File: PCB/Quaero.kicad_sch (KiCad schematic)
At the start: 61 parts, among them J1 USB_C_Receptacle_USB2.0_16P, J2 OLED_128x32, J5 Conn_01x02, SW2 SW_SPDT

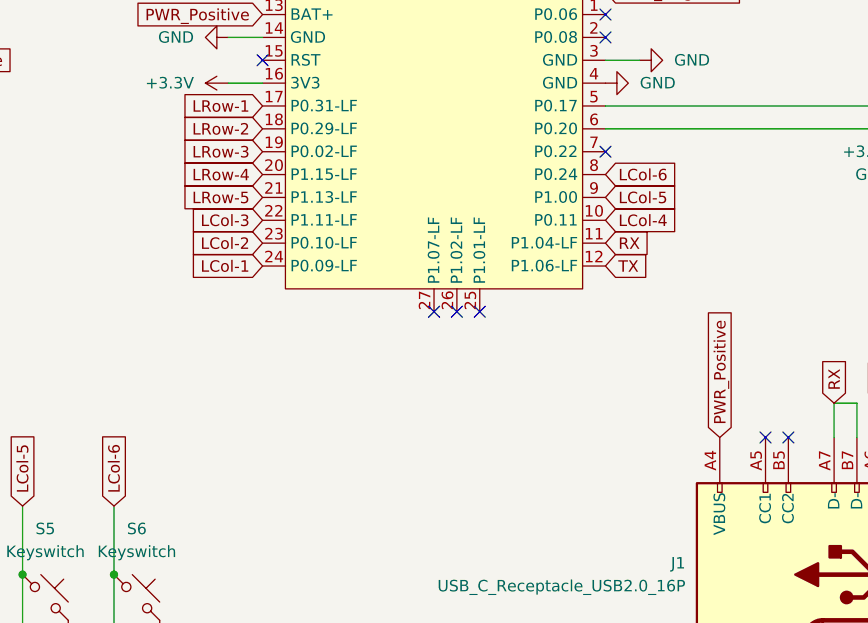
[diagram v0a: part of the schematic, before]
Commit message: Left side partial routing attempt 4
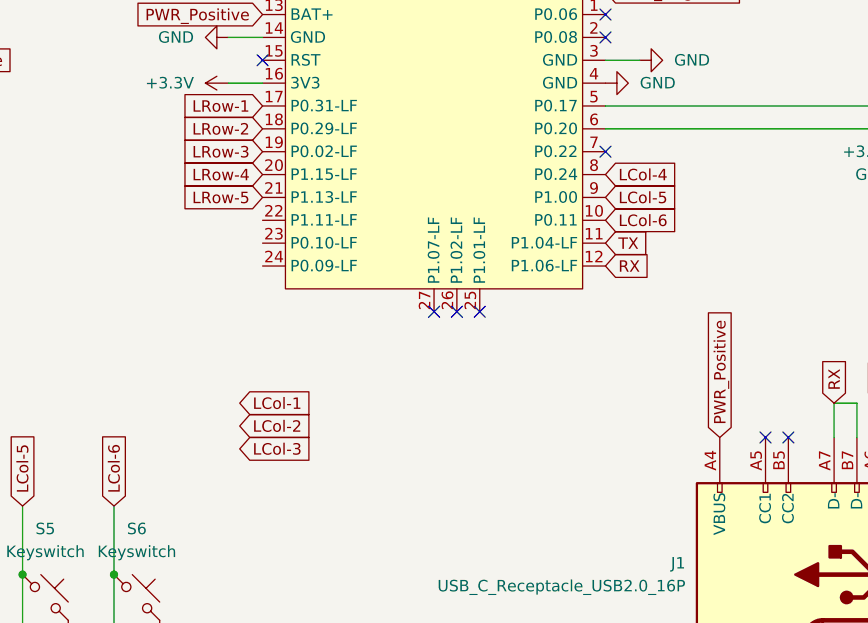
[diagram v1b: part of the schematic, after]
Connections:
- net LCol-1: no longer MCUL1.24 (P0.09-LF)
- net LCol-2: no longer MCUL1.23 (P0.10-LF)
- net LCol-3: no longer MCUL1.22 (P1.11-LF)
- net LCol-4: now also MCUL1.8 (P0.24); no longer MCUL1.10 (P0.11)
- net LCol-6: now also MCUL1.10 (P0.11); no longer MCUL1.8 (P0.24)
- net RX: now also MCUL1.12 (P1.06-LF); no longer MCUL1.11 (P1.04-LF)
- net TX: now also MCUL1.11 (P1.04-LF); no longer MCUL1.12 (P1.06-LF)

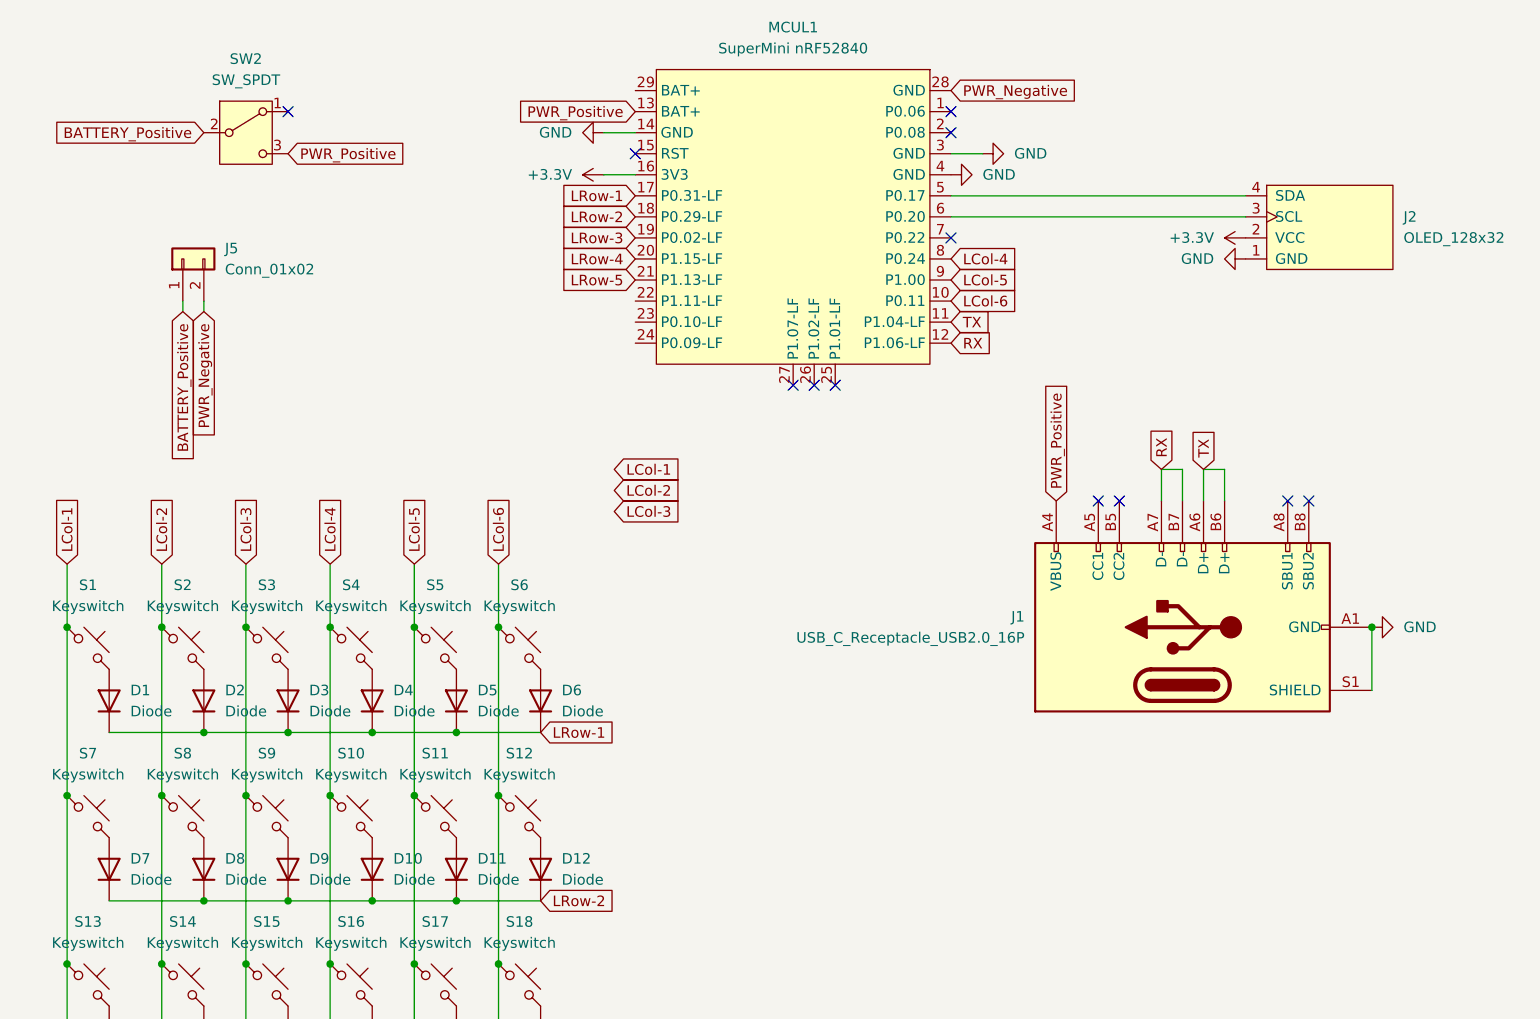
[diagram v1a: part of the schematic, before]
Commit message: Updated to RP2040, routing columns attempt 1
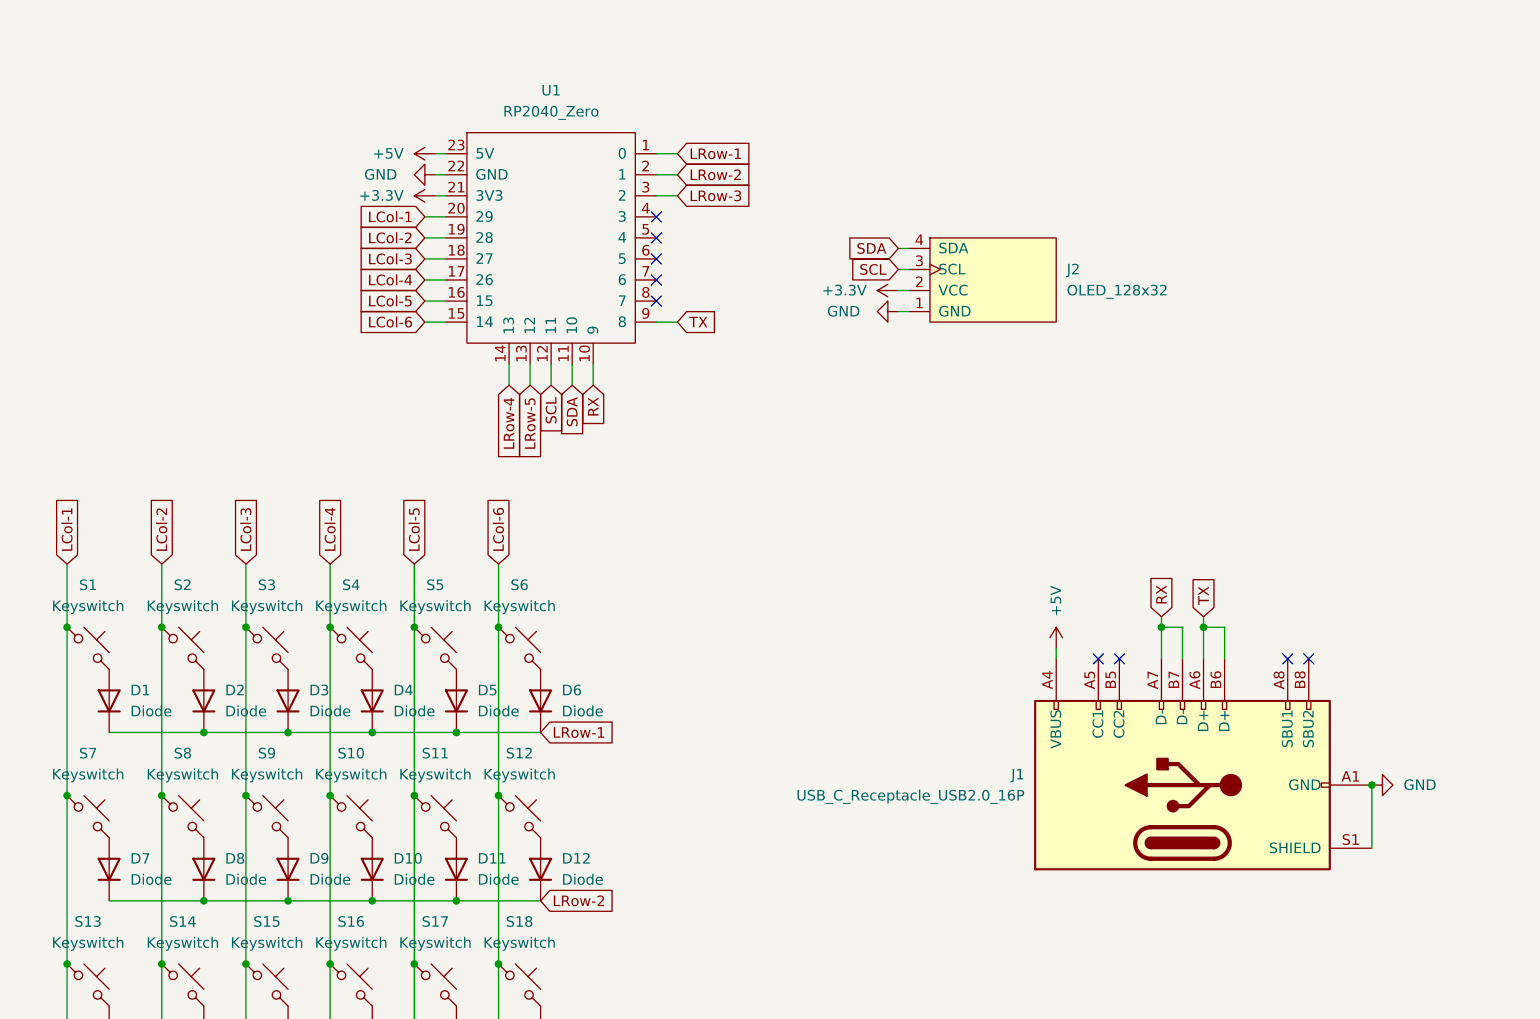
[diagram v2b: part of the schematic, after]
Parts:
- removed J5: Conn_01x02, Connector_JST:JST_PH_S2B-PH-K_1x02_P2.00mm_Horizontal, symbol Connector_Generic:Conn_01x02
- removed MCUL1: SuperMini nRF52840, marbastlib-xp-promicroish:SuperMini_nRF52840_AH_USBdn, symbol marbastlib-promicroish:SuperMini_nRF52840
- removed SW2: SW_SPDT, marbastlib-various:SW_MSK12C02-HB, symbol Switch:SW_SPDT
- added U1: RP2040_Zero, ScottoKeebs_MCU:RP2040_Zero, symbol ScottoKeebs:MCU_RP2040_Zero
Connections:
- net +3.3V: now also U1.21 (3V3)
- net GND: now also U1.22 (GND)
- net LCol-1: now also U1.20 (29)
- net LCol-2: now also U1.19 (28)
- net LCol-3: now also U1.18 (27)
- net LCol-4: now also U1.17 (26)
- net LCol-5: now also U1.16 (15)
- net LCol-6: now also U1.15 (14)
- net LRow-1: now also U1.1 (0)
- net LRow-2: now also U1.2 (1)
- net LRow-3: now also U1.3 (2)
- net LRow-4: now also U1.14 (13)
- net LRow-5: now also U1.13 (12)
- net RX: now also U1.10 (9)
- net TX: now also U1.9 (8)
- net SDA: now reaches J2.4 (SDA)
- net SDA: now also U1.11 (10)
- net SCL: now reaches J2.3 (SCL)
- net SCL: now also U1.12 (11)
- net PWR_Positive renamed +5V
- net +5V: now also U1.23 (5V)
- no-connect marks 12 -> 9
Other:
- moved on the sheet: J1

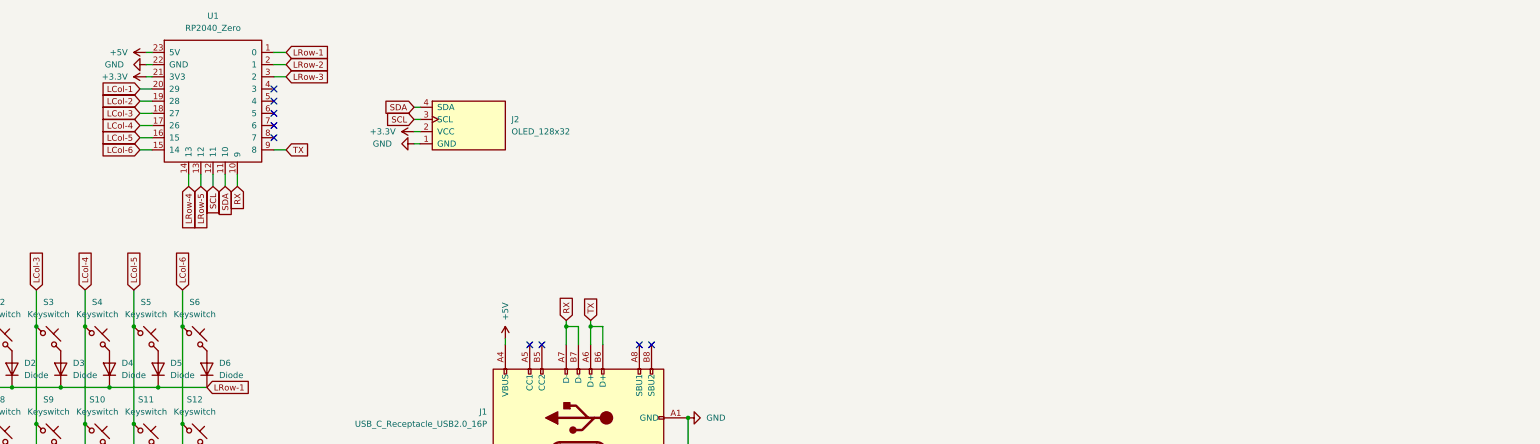
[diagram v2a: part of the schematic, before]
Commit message: Revised routing, changed the MCU to the RP2040 Zero, changed the USB-C schematic
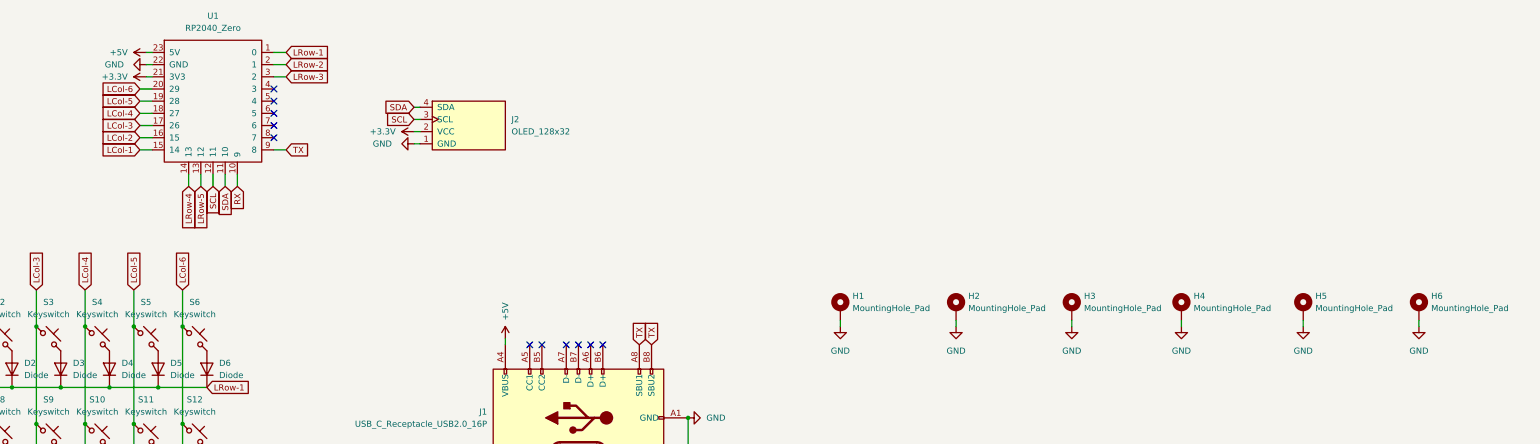
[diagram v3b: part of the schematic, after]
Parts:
- added H1, H2, H3, H4, H5, H6: MountingHole_Pad, MountingHole:MountingHole_2.2mm_M2_DIN965_Pad, symbol Mechanical:MountingHole_Pad
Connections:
- net GND: now also H1.1, H2.1, H3.1, H4.1, H5.1, H6.1
- net LCol-1: now also U1.15 (14); no longer U1.20 (29)
- net LCol-2: now also U1.16 (15); no longer U1.19 (28)
- net LCol-3: now also U1.17 (26); no longer U1.18 (27)
- net LCol-4: now also U1.18 (27); no longer U1.17 (26)
- net LCol-5: now also U1.19 (28); no longer U1.16 (15)
- net LCol-6: now also U1.20 (29); no longer U1.15 (14)
- net RX: no longer J1.A7 (D-), J1.B7 (D-)
- net TX: now also J1.A8 (SBU1), J1.B8 (SBU2); no longer J1.A6 (D+), J1.B6 (D+)
- no-connect marks 9 -> 11

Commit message: Safety commit before flipping rp2040
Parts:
- added H10, H7, H8, H9: MountingHole_Pad, MountingHole:MountingHole_2.2mm_M2_Pad, symbol Mechanical:MountingHole_Pad
- H1, H2, H3, H4, H5, H6: footprint MountingHole:MountingHole_2.2mm_M2_DIN965_Pad -> MountingHole:MountingHole_2.2mm_M2_Pad
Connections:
- net GND: now also H10.1, H7.1, H8.1, H9.1
- net RX: now also J1.A6 (D+), J1.B6 (D+)
- net TX: now also J1.A7 (D-), J1.B7 (D-); no longer J1.A8 (SBU1), J1.B8 (SBU2)
- no-connect marks 11 -> 10
